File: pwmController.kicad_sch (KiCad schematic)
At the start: 0 parts

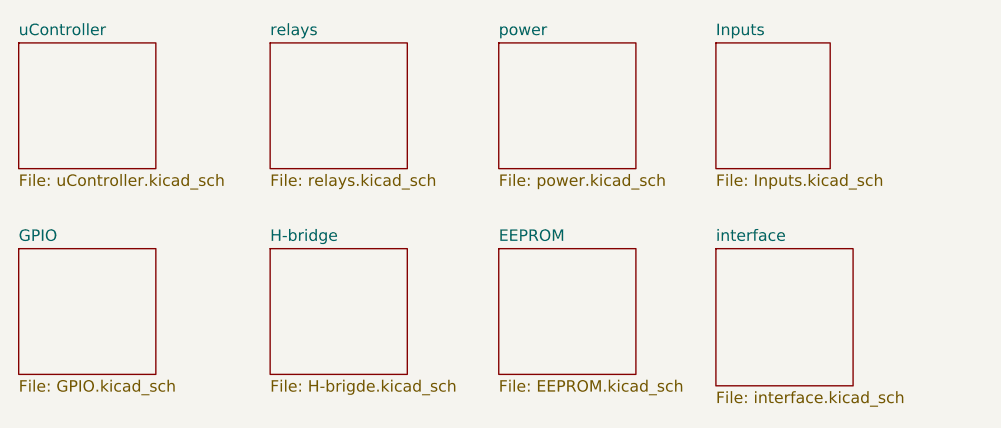
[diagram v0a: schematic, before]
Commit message: redid this project. I want to use an atmega328 so I ditched some IO. I retained 4 servo, 1 H-bridge (should make it double), 3 relays, 6 GPIO, 1 potentiometer and loconet interface. And I still have a config button
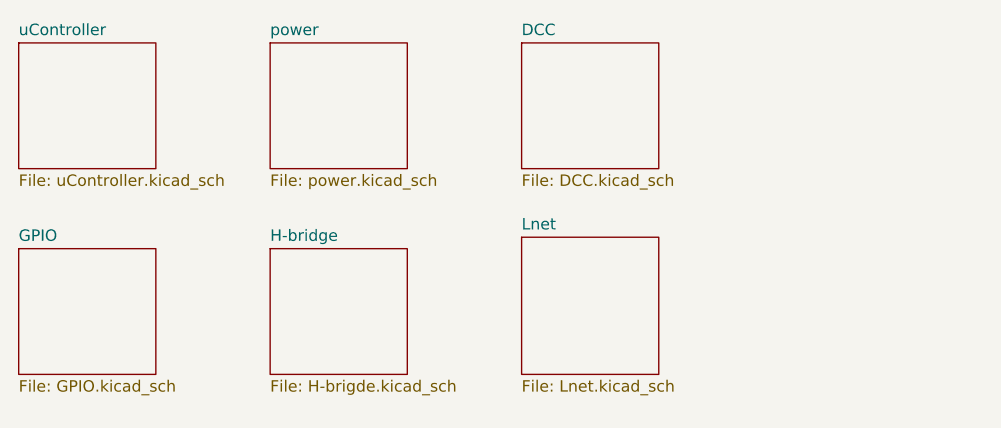
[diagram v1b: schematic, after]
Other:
- sheet interface renamed Lnet
- removed sheet EEPROM
- removed sheet Inputs
- removed sheet relays
- added sheet DCC (DCC.kicad_sch)
- sheet Lnet: file interface.kicad_sch -> Lnet.kicad_sch
